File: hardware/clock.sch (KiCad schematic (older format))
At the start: 18 parts

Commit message: more work on tdr schematic
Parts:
- removed C?: .01 uF, symbol Device:C_Small
- removed R?: JMP, symbol Device:R_Small
- removed R? (x4): DNP, symbol Device:R_Small
- removed U?: SY89329V, symbol synth_lib:SY89329V
- added C? (x4): 100 nF, symbol Device:C_Small
- added C? (x4): 100 pF, symbol Device:C_Small
- added C?: DNP, symbol Device:C_Small
- added C? (x5): .01 uF, symbol Device:C_Small
- added L?: L_Small, symbol Device:L_Small
- added R? (x2): 50, symbol Device:R_Small
- added R? (x3): JMP, symbol Device:R_Small
- added R?: 68, symbol Device:R_Small
- added R? (x3): 1k, symbol Device:R_Small
- added R?: DNP, symbol Device:R_Small
- added R? (x4): 125, symbol Device:R_Small
- added R? (x4): 84, symbol Device:R_Small
- added R?: TBD, symbol Device:R_Small
- added R?: DNI, symbol Device:R_Small
- added TP?: TestPoint, symbol Connector:TestPoint
- added U?: ICS853S057I, symbol tdr:ICS853S057I
- added U?: ADCMP580, symbol tdr-rescue:ADCMP580-synth_lib
- added U?: SY89321L-synth_lib, symbol tdr-rescue:SY89321L-synth_lib
- R?: value 50 -> 1k
- U?: symbol synth_lib:CDCLVP1204 -> tdr-rescue:CDCLVP1204-synth_lib
- X?: symbol synth_lib:DV75D_TCXO -> tdr-rescue:DV75D_TCXO-synth_lib
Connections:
- net labels added: -5VA, ANALOG_TRIG_INPUT, ANALOG_TRIG_REF, CLK_FPGA, TRIG_SEL0, TRIG_SEL1
- net labels removed: CLK_FPGA_N, CLK_FPGA_P
- wire segments 79 -> 205
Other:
- note added: "+/- 2V"
- note added: "50 ohm input impedance"
- note added: "EXT ANALOG TRIG"
- note added: "EXT TRIG PULSE"
- note added: "LVCMOS"
- note added: "LVPECL OUTPUT"
- note added: "LVPECL TERMINATION"
- note added: "TODO:VERIFY PECL/LVPECL COMPATIBILITY"
- note removed: "20 mA"
- note removed: "EXTERNAL TRIGGER"
- moved on the sheet: C?, R?, TP?

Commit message: work on tdr schematic..
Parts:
- U?: symbol tdr-rescue:CDCLVP1204-synth_lib -> tdr-rescue:CDCLVP1204-synth_lib-tdr-rescue
- U?: symbol tdr:ICS853S057I -> tdr-rescue:ICS853S057I-tdr
- U?: symbol tdr-rescue:ADCMP580-synth_lib -> tdr-rescue:ADCMP580-synth_lib-tdr-rescue
- U?: symbol tdr-rescue:SY89321L-synth_lib -> tdr-rescue:SY89321L-synth_lib-tdr-rescue
- X?: symbol tdr-rescue:DV75D_TCXO-synth_lib -> tdr-rescue:DV75D_TCXO-synth_lib-tdr-rescue
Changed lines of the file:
@@
 $Descr A3 16535 11693
 encoding utf-8
-Sheet 3 9
+Sheet 3 8
 Title ""
 Date ""
@@
 $EndDescr
 $Comp
-L tdr-rescue:DV75D_TCXO-synth_lib X?
+L tdr-rescue:DV75D_TCXO-synth_lib-tdr-rescue X?
 U 1 1 5BC18539
 P 5050 4150
@@
 	5300 3250 5300 3350
 $Comp
-L tdr-rescue:CDCLVP1204-synth_lib U?
+L tdr-rescue:CDCLVP1204-synth_lib-tdr-rescue U?
 U 1 1 5BC1E724
 P 7700 4300
@@
 LVPECL OUTPUT
 $Comp
-L tdr-rescue:SY89321L-synth_lib U?
+L tdr-rescue:SY89321L-synth_lib-tdr-rescue U?
 U 1 1 5BFD7F17
 P 11800 3850
@@
 EXT ANALOG TRIG
 $Comp
-L tdr:ICS853S057I U?
+L tdr-rescue:ICS853S057I-tdr U?
 U 1 1 5BE3EFE8
 P 11850 6500
+AR Path="/5BE3EFE8" Ref="U?"  Part="1"
+AR Path="/5BC3F72A/5BE3EFE8" Ref="U?"  Part="1"
 F 0 "U?" H 11850 7215 50  0000 C CNN
 F 1 "ICS853S057I" H 11850 7124 50  0000 C CNN
@@
 LVPECL TERMINATION
 $Comp
-L tdr-rescue:ADCMP580-synth_lib U?
+L tdr-rescue:ADCMP580-synth_lib-tdr-rescue U?
 U 1 1 5BF5E6BE
 P 3250 6600

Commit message: footprint assignment
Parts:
- added C319: 10 pF, Capacitors_SMD:C_0402, symbol Device:C_Small
- added C320: 100 nF, Capacitors_SMD:C_0402, symbol Device:C_Small
- added TP303, TP304: TestPoint, vna_footprints:TP07R, symbol Connector:TestPoint
- C301, C302, C303, C305, C306, C307, C308, C309, C310, C311, C312, C313, C314, C315, C316, C317, C318: renamed from C?; footprint (none) -> Capacitors_SMD:C_0402
- C304: renamed from C?; value 100 nF -> 10 nF; footprint (none) -> Capacitors_SMD:C_0402
- L301: renamed from L?; footprint (none) -> Resistors_SMD:R_0402
- R301, R302, R303, R304, R305, R306, R307, R308, R309, R310, R311, R312, R313, R314, R315, R316, R317, R318, R319, R320, R321, R322, R323, R324: renamed from R?; footprint (none) -> Resistors_SMD:R_0402
- TP301, TP302: renamed from TP?; footprint (none) -> vna_footprints:TP07R
- U301, U302: renamed from U?; footprint (none) -> Housings_DFN_QFN:UQFN-16-1EP_3x3mm_Pitch0.5mm
- U303: renamed from U?; footprint (none) -> Housings_DFN_QFN:DFN-8-1EP_2x2mm_Pitch0.5mm
- U304: renamed from U?; footprint (none) -> Housings_SSOP:TSSOP-20_4.4x6.5mm_Pitch0.65mm
- X301: renamed from X?; footprint (none) -> vna_footprints:DV75D
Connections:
- net +3V3: now also U304.14 (Vcc), C320.1
- net GND: now also C319.2, C320.2
- net at R306.1, X301.3 (OUT): now also C319.1
- net at U304.12 (Vbb2): now also TP304.1
- net at U304.13 (Vbb1): now also TP303.1
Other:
- note added: "NOT USED WITH LVPECL\n"
- moved on the sheet: C304, X301

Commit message: work on tdr component placement
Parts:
- added C321, C323: 100 pF, Capacitors_SMD:C_0402, symbol Device:C_Small
- added C322, C324, C325: 2.2 uF, Capacitors_SMD:C_0603, symbol Device:C_Small
- added R325: 125, Resistors_SMD:R_0402, symbol Device:R_Small
- added TP305, TP306: TestPoint, vna_footprints:TP07R, symbol Connector:TestPoint
- C301, C303: value .01 uF -> 10 nF
- R321: value 50 -> 125
- R322: value 50 -> 84
- R323: value 68 -> 84
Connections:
- net +3V3: now also R321.1, C325.1, R325.1
- net +5VA: now also C321.1, C322.1
- net -5VA: now also C323.1, C324.1
- net GND: now also R322.2, C321.2, C322.2, C323.2, C324.2, C325.2
- net at U302.10 (OUTN0), U303.3 (~IN): now also R322.1, R325.2; no longer R322.2
- net at U302.9 (OUTP0), U303.2 (IN): now also R321.2, R323.2; no longer R321.1
- net CLK_DAC_N: no longer names the net of U302.12 (OUTN1)
- net CLK_DAC_N: now also TP306.1
- net CLK_DAC_P: no longer names the net of U302.11 (OUTP1)
- net CLK_DAC_P: now also TP305.1
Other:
- note added: "EXT FPGA CLOCK BUFFER"
- note added: "TRIGGER SOURCE SELECT MUX\n0 - 10 MHZ CLK\n1 - UNUSED\n2 - ANALOG TRIGGER\n3 - EXT PULSE"
- note added: "UNUSED OUTPUTS\nCAN BE LEFT FLOATING\n"
- moved on the sheet: R321, R322, R323

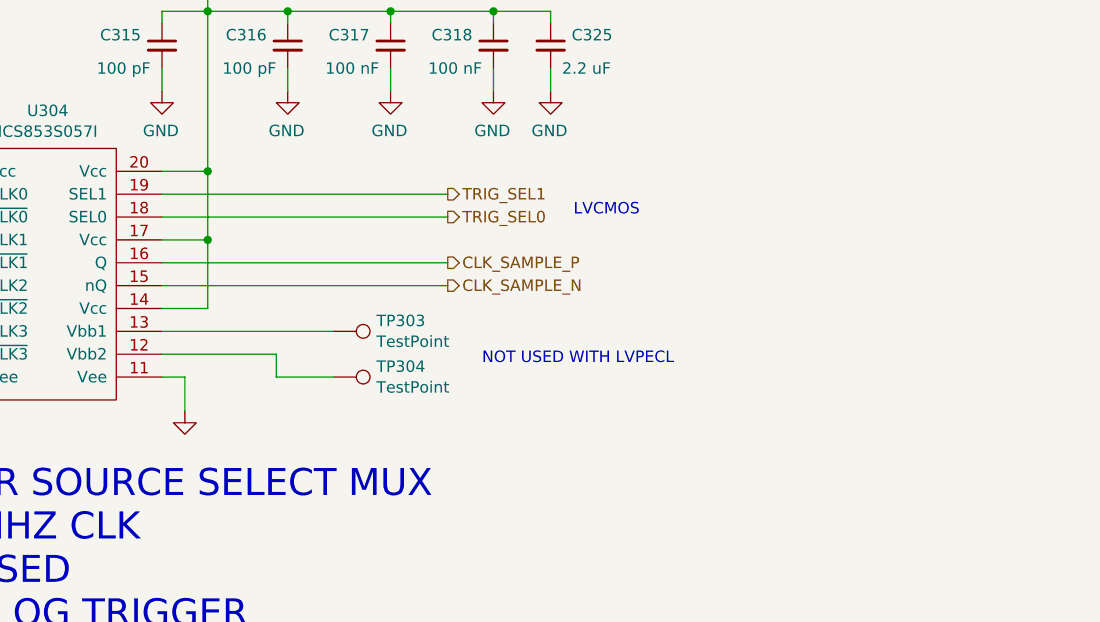
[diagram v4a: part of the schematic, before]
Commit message: added rf crossover for latch trigger line to help with layout
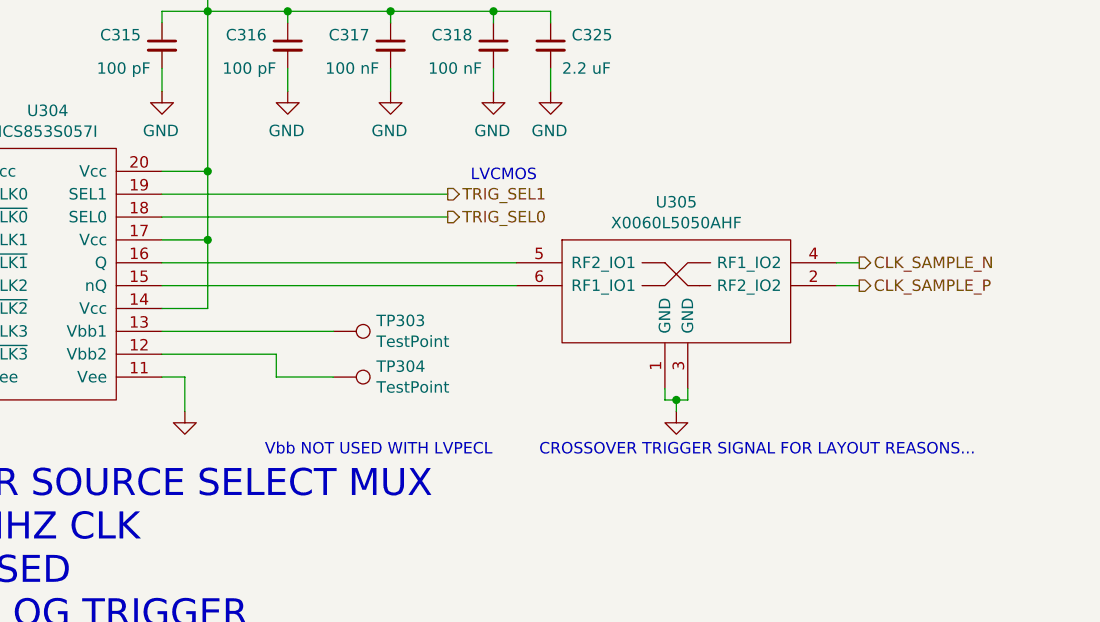
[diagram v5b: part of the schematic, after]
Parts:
- added U305: X0060L5050AHF, synth_footprints:X0060L5050AHF, symbol synth_lib:X0060L5050AHF
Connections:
- net CLK_SAMPLE_N: now also U305.4 (RF1_IO2); no longer U304.15 (nQ)
- net CLK_SAMPLE_P: now also U305.2 (RF2_IO2); no longer U304.16 (Q)
- net GND: now also U305.1 (GND), U305.3 (GND)
- new net: U304.15 (nQ), U305.6 (RF1_IO1)
- new net: U304.16 (Q), U305.5 (RF2_IO1)
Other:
- note added: "CROSSOVER TRIGGER SIGNAL FOR LAYOUT REASONS..."
- note added: "Vbb NOT USED WITH LVPECL\n"
- note removed: "NOT USED WITH LVPECL\n"
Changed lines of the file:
@@
 	7050 4700 7050 4800
 Connection ~ 7050 4800
-Text HLabel 13600 6550 2    50   Output ~ 0
+Text HLabel 15400 6450 2    50   Output ~ 0
 CLK_SAMPLE_N
-Text HLabel 13600 6450 2    50   Output ~ 0
+Text HLabel 15400 6550 2    50   Output ~ 0
 CLK_SAMPLE_P
 Wire Wire Line
@@
 	1    0    0    -1
 $EndComp
-Wire Wire Line
-	12350 6450 13600 6450
-Wire Wire Line
-	12350 6550 13600 6550
 $Comp
 L Device:C_Small C310
@@
 Text HLabel 13600 6250 2    50   Output ~ 0
 TRIG_SEL0
-Text Notes 14150 6250 0    50   ~ 0
+Text Notes 13700 6100 0    50   ~ 0
 LVCMOS
 Wire Wire Line
@@
 Wire Wire Line
 	12850 6950 13100 6950
-Text Notes 13750 6900 0    50   ~ 0
-NOT USED WITH LVPECL\n
+Text Notes 12800 7300 0    50   ~ 0
+Vbb NOT USED WITH LVPECL\n
 Wire Wire Line
 	5050 4150 5200 4150
@@
 Text Notes 9000 4200 0    50   ~ 0
 UNUSED OUTPUTS\nCAN BE LEFT FLOATING\n
+Text Notes 14000 7300 0    50   ~ 0
+CROSSOVER TRIGGER SIGNAL FOR LAYOUT REASONS...
+Wire Wire Line
+	12350 6550 13900 6550
+Wire Wire Line
+	12350 6450 13900 6450
+Wire Wire Line
+	15300 6450 15400 6450
+Wire Wire Line
+	15300 6550 15400 6550
+$Comp
+L power:GND #PWR?
+U 1 1 5C43D240
+P 14600 7100
+AR Path="/5BC41CC8/5C43D240" Ref="#PWR?"  Part="1"
+AR Path="/5BC3F72A/5C43D240" Ref="#PWR0152"  Part="1"
+F 0 "#PWR0152" H 14600 6850 50  0001 C CNN
+F 1 "GND" V 14605 6972 50  0001 R CNN
+F 2 "" H 14600 7100 50  0001 C CNN
+F 3 "" H 14600 7100 50  0001 C CNN
+	1    14600 7100
+	-1   0    0    -1
+$EndComp
+Wire Wire Line
+	14600 7100 14600 7050
+Wire Wire Line
+	14600 7050 14550 7050
+Wire Wire Line
+	14550 7050 14550 7000
+Wire Wire Line
+	14600 7050 14650 7050
+Wire Wire Line
+	14650 7050 14650 7000
+Connection ~ 14600 7050
+$Comp
+L synth_lib:X0060L5050AHF U305
+U 1 1 5C49FCBC
+P 14600 6500
+F 0 "U305" H 14600 6815 50  0000 C CNN
+F 1 "X0060L5050AHF" H 14600 6724 50  0000 C CNN
+F 2 "synth_footprints:X0060L5050AHF" H 14600 6500 50  0001 C CNN
+F 3 "" H 14600 6500 50  0001 C CNN
+	1    14600 6500
+	1    0    0    -1
+$EndComp
 $EndSCHEMATC

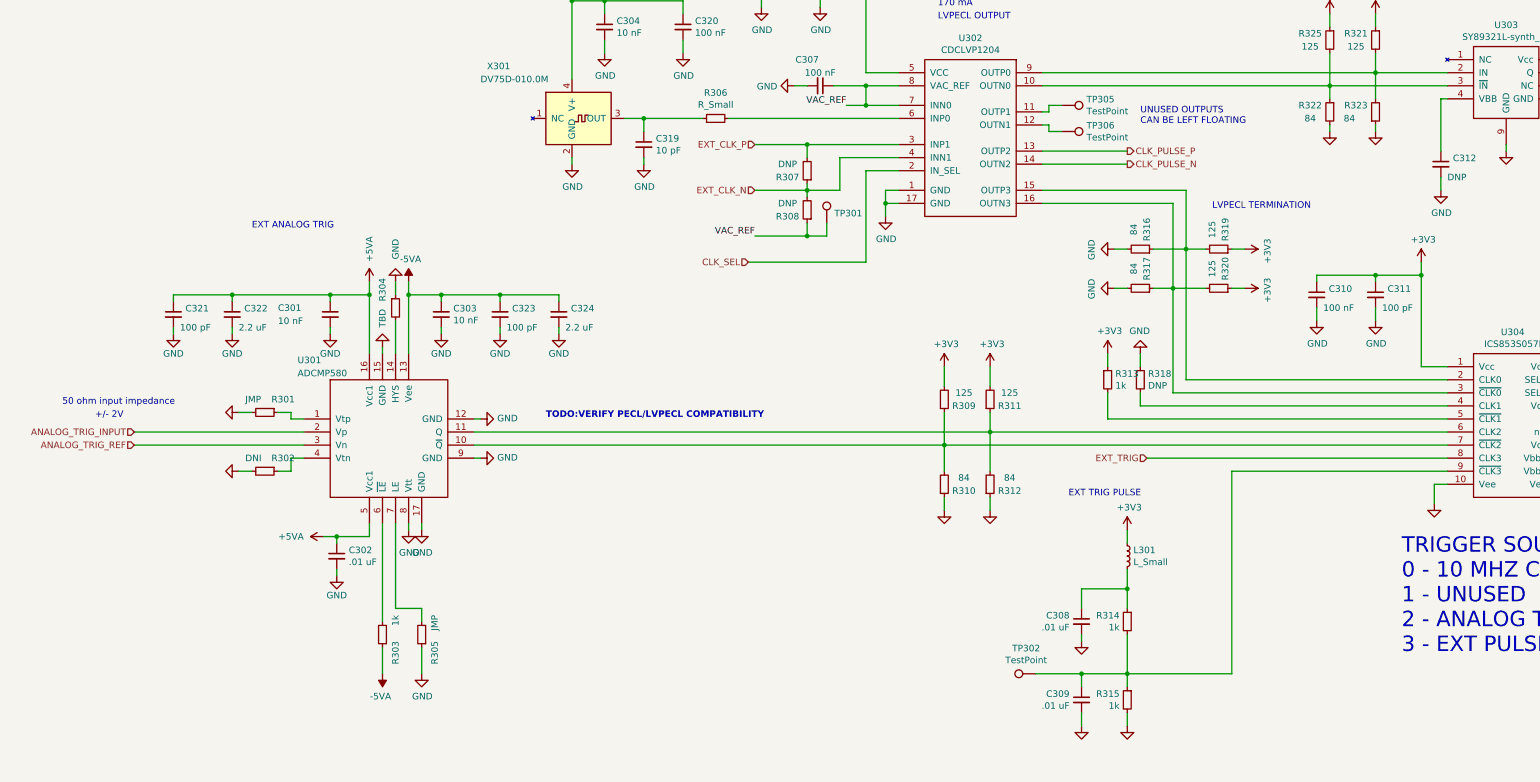
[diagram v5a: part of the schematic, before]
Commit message: more component placement on tdr..
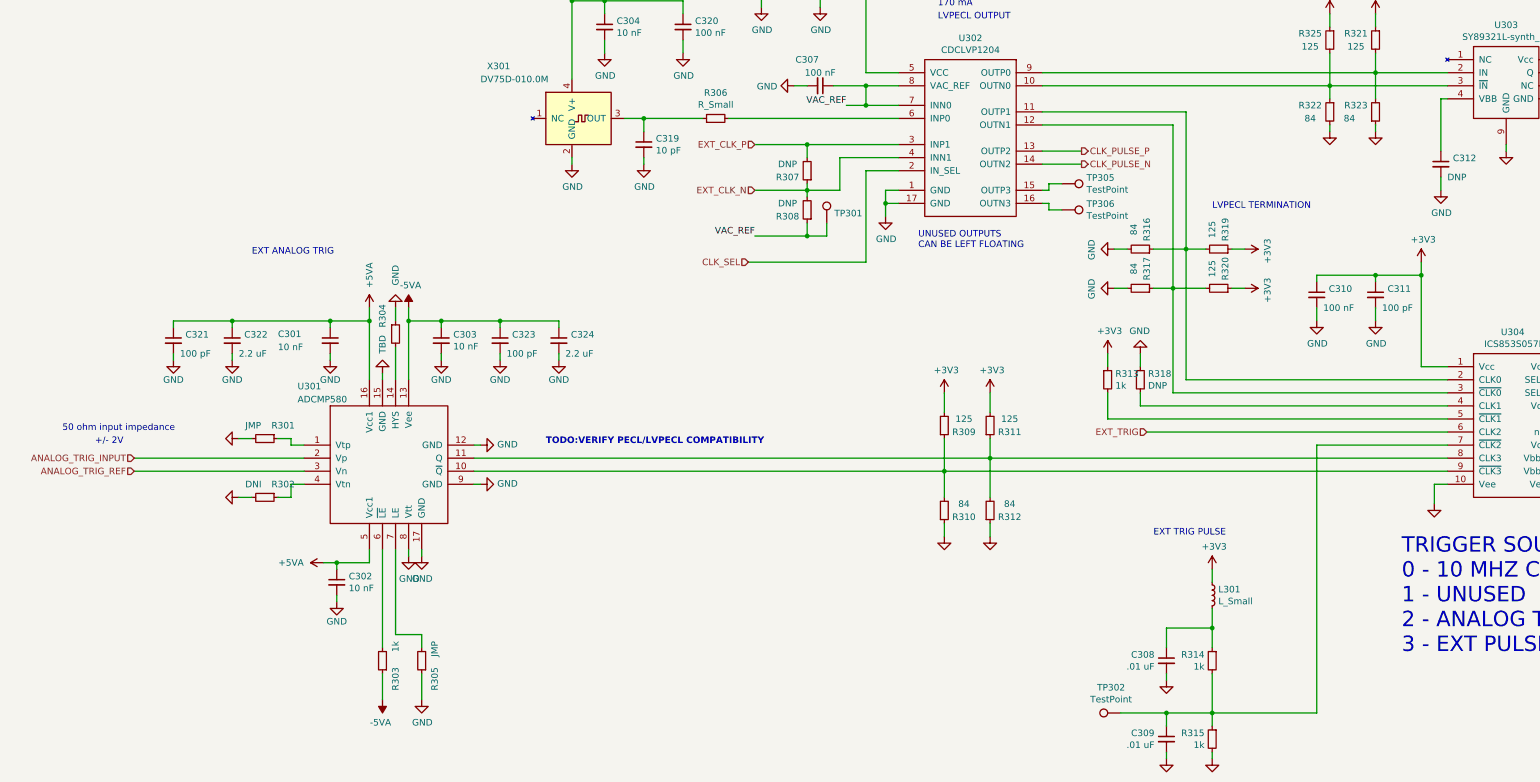
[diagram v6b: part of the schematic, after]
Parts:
- C302: value .01 uF -> 10 nF
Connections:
- net EXT_TRIG: now also U304.6 (CLK2); no longer U304.8 (CLK3)
- net at U302.11 (OUTP1): now also R316.1, R319.2, U304.2 (CLK0); no longer TP305.1
- net at U302.12 (OUTN1): now also R317.1, R320.2, U304.3 (~CLK0); no longer TP306.1
- net at C309.1, R314.2, R315.1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: now also U304.7 (~CLK2); no longer U304.9 (~CLK3)
- net at R311.1, R312.2, U301.11 (Q): now also U304.8 (CLK3); no longer U304.6 (CLK2)
- net at R309.1, R310.2, U301.10 (~Q): now also U304.9 (~CLK3); no longer U304.7 (~CLK2)
- new net: TP305.1, U302.15 (OUTP3)
- new net: TP306.1, U302.16 (OUTN3)
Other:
- moved on the sheet: C301, C302, C303, C308, C309, C321, C322, C323, C324, L301, R301, R302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

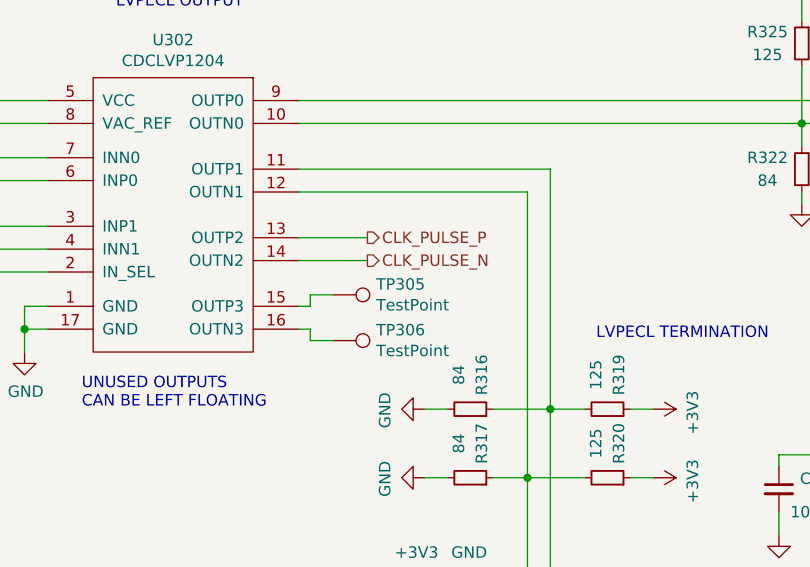
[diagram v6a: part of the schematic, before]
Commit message: routing high speed digital
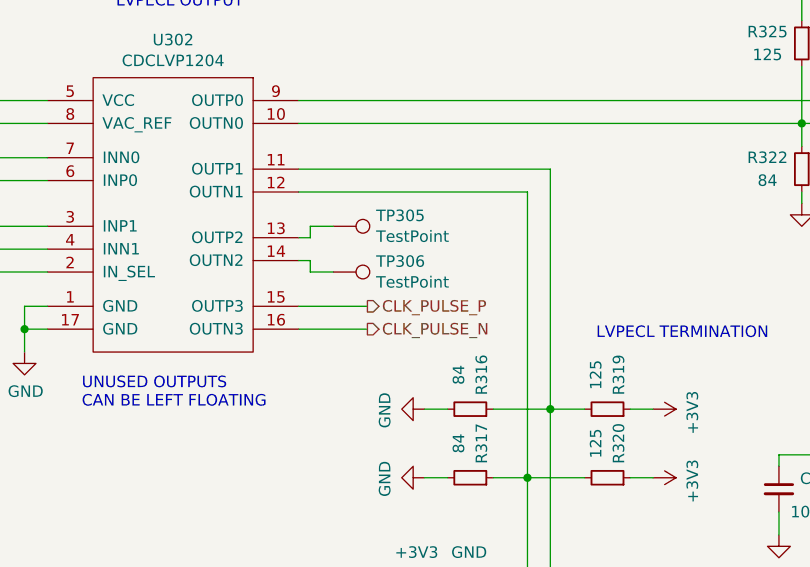
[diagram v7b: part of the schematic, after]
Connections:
- net CLK_PULSE_N: now also U302.16 (OUTN3); no longer U302.14 (OUTN2)
- net CLK_PULSE_P: now also U302.15 (OUTP3); no longer U302.13 (OUTP2)
- net at TP305.1: now also U302.13 (OUTP2); no longer U302.15 (OUTP3)
- net at TP306.1: now also U302.14 (OUTN2); no longer U302.16 (OUTN3)
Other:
- moved on the sheet: TP305, TP306
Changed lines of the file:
@@
 Text HLabel 13150 3800 2    50   Output ~ 0
 CLK_FPGA
-Text HLabel 8550 4400 2    50   Output ~ 0
+Text HLabel 8550 4700 2    50   Output ~ 0
 CLK_PULSE_P
-Text HLabel 8550 4500 2    50   Output ~ 0
+Text HLabel 8550 4800 2    50   Output ~ 0
 CLK_PULSE_N
 $Comp
@@
 L Connector:TestPoint TP305
 U 1 1 5C33EF85
-P 8400 4650
-F 0 "TP305" V 8354 4838 50  0000 L CNN
-F 1 "TestPoint" V 8445 4838 50  0000 L CNN
-F 2 "vna_footprints:TP07R" H 8600 4650 50  0001 C CNN
-F 3 "~" H 8600 4650 50  0001 C CNN
-	1    8400 4650
+P 8400 4350
+F 0 "TP305" V 8354 4538 50  0000 L CNN
+F 1 "TestPoint" V 8445 4538 50  0000 L CNN
+F 2 "vna_footprints:TP07R" H 8600 4350 50  0001 C CNN
+F 3 "~" H 8600 4350 50  0001 C CNN
+	1    8400 4350
 	0    1    1    0
 $EndComp
@@
 L Connector:TestPoint TP306
 U 1 1 5C33F1E6
-P 8400 4850
-F 0 "TP306" V 8354 5038 50  0000 L CNN
-F 1 "TestPoint" V 8445 5038 50  0000 L CNN
-F 2 "vna_footprints:TP07R" H 8600 4850 50  0001 C CNN
-F 3 "~" H 8600 4850 50  0001 C CNN
-	1    8400 4850
+P 8400 4550
+F 0 "TP306" V 8354 4738 50  0000 L CNN
+F 1 "TestPoint" V 8445 4738 50  0000 L CNN
+F 2 "vna_footprints:TP07R" H 8600 4550 50  0001 C CNN
+F 3 "~" H 8600 4550 50  0001 C CNN
+	1    8400 4550
 	0    1    1    0
 $EndComp
 Wire Wire Line
-	8250 4700 8300 4700
-Wire Wire Line
-	8300 4700 8300 4650
-Wire Wire Line
-	8300 4650 8400 4650
-Wire Wire Line
-	8250 4800 8300 4800
-Wire Wire Line
-	8300 4800 8300 4850
-Wire Wire Line
-	8300 4850 8400 4850
+	8250 4400 8300 4400
+Wire Wire Line
+	8300 4400 8300 4350
+Wire Wire Line
+	8300 4350 8400 4350
+Wire Wire Line
+	8250 4500 8300 4500
+Wire Wire Line
+	8300 4500 8300 4550
+Wire Wire Line
+	8300 4550 8400 4550
 Text Notes 7300 5150 0    50   ~ 0
 UNUSED OUTPUTS\nCAN BE LEFT FLOATING\n
@@
 	9350 4100 9350 5150
 Wire Wire Line
-	8550 4400 8250 4400
-Wire Wire Line
-	8250 4500 8550 4500
+	8550 4700 8250 4700
+Wire Wire Line
+	8250 4800 8550 4800
 $EndSCHEMATC
